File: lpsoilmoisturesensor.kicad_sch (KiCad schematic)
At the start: 5 parts, among them J1 Conn_01x03

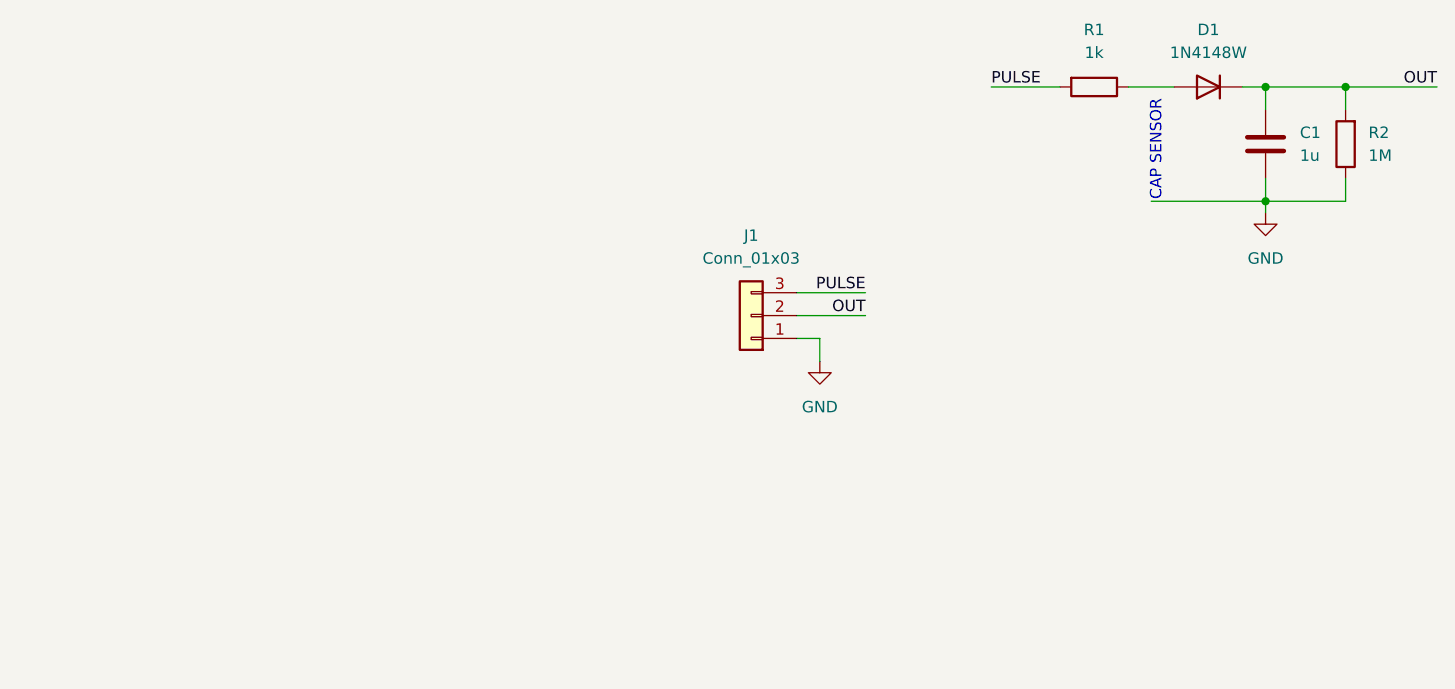
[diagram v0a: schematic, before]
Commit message: rebuild in kicad v6
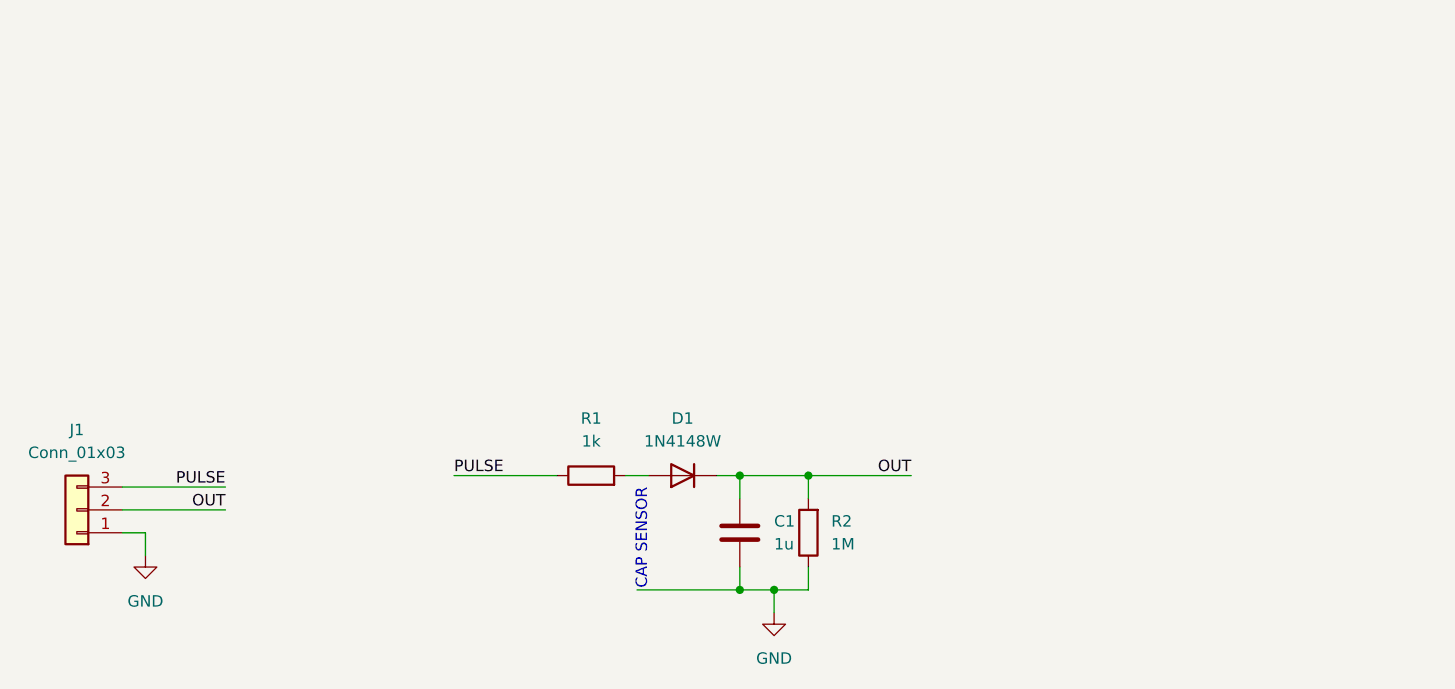
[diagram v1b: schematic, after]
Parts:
- removed D1: 1N4148W, Diode_SMD:D_SOD-123, symbol Diode:1N4148W
- added D1: 1N4148W, Diode_SMD:D_SOD-123, symbol Device:D
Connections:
- net GND: now also C1.2; no longer C1.1
- net OUT: now also C1.1, D1.1 (K); no longer C1.2
- net PULSE: now also R1.1; no longer R1.2
- new net: D1.2 (A), R1.2
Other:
- company: Philipp Tebbe -> (none)
- title: Low Power Soil Moisture Sensor -> (none)
